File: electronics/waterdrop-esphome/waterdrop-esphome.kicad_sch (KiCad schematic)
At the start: 27 parts, among them J1 12V_IN, J2 12V_OUT, J3 Comm_RO, J4 Comm_Faucet, J5 Valve, K1 G5LE-1, Q1 BC817, U2 ESP32-S3-Tiny, U3 74AHCT125, U4 TB67H450A

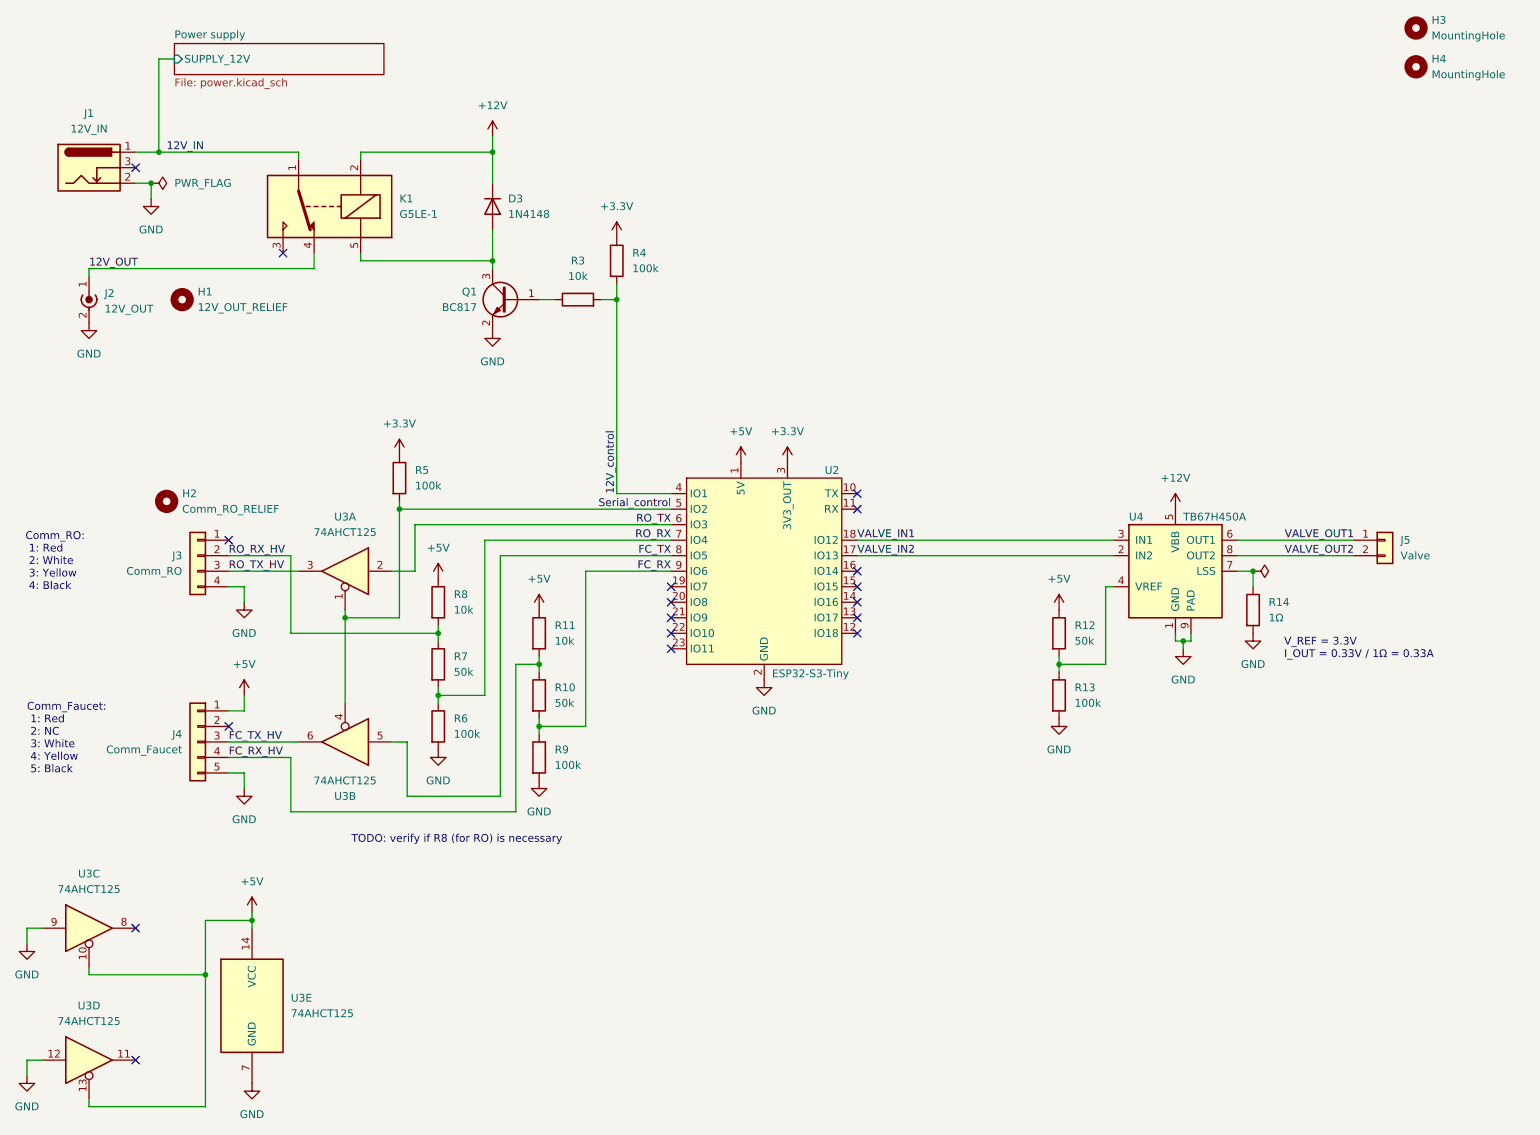
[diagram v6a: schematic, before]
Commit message: Schematics: apply verified 0.1 fixes: - Bump version to 0.2 - Change mounting holes to M3 - 12 -> 24V input voltage:   - C1: 16V -> 50V   - D1: SMAJ13A -> SMAJ30A   - D2: B220A -> B360A   - K1: G5LE-1 -> G5LE-1-E DC24 - R4: 100k -> 47k (it was too weak to fully open relay transistor) - R7/R10/R12: 50k -> 51k (more common)
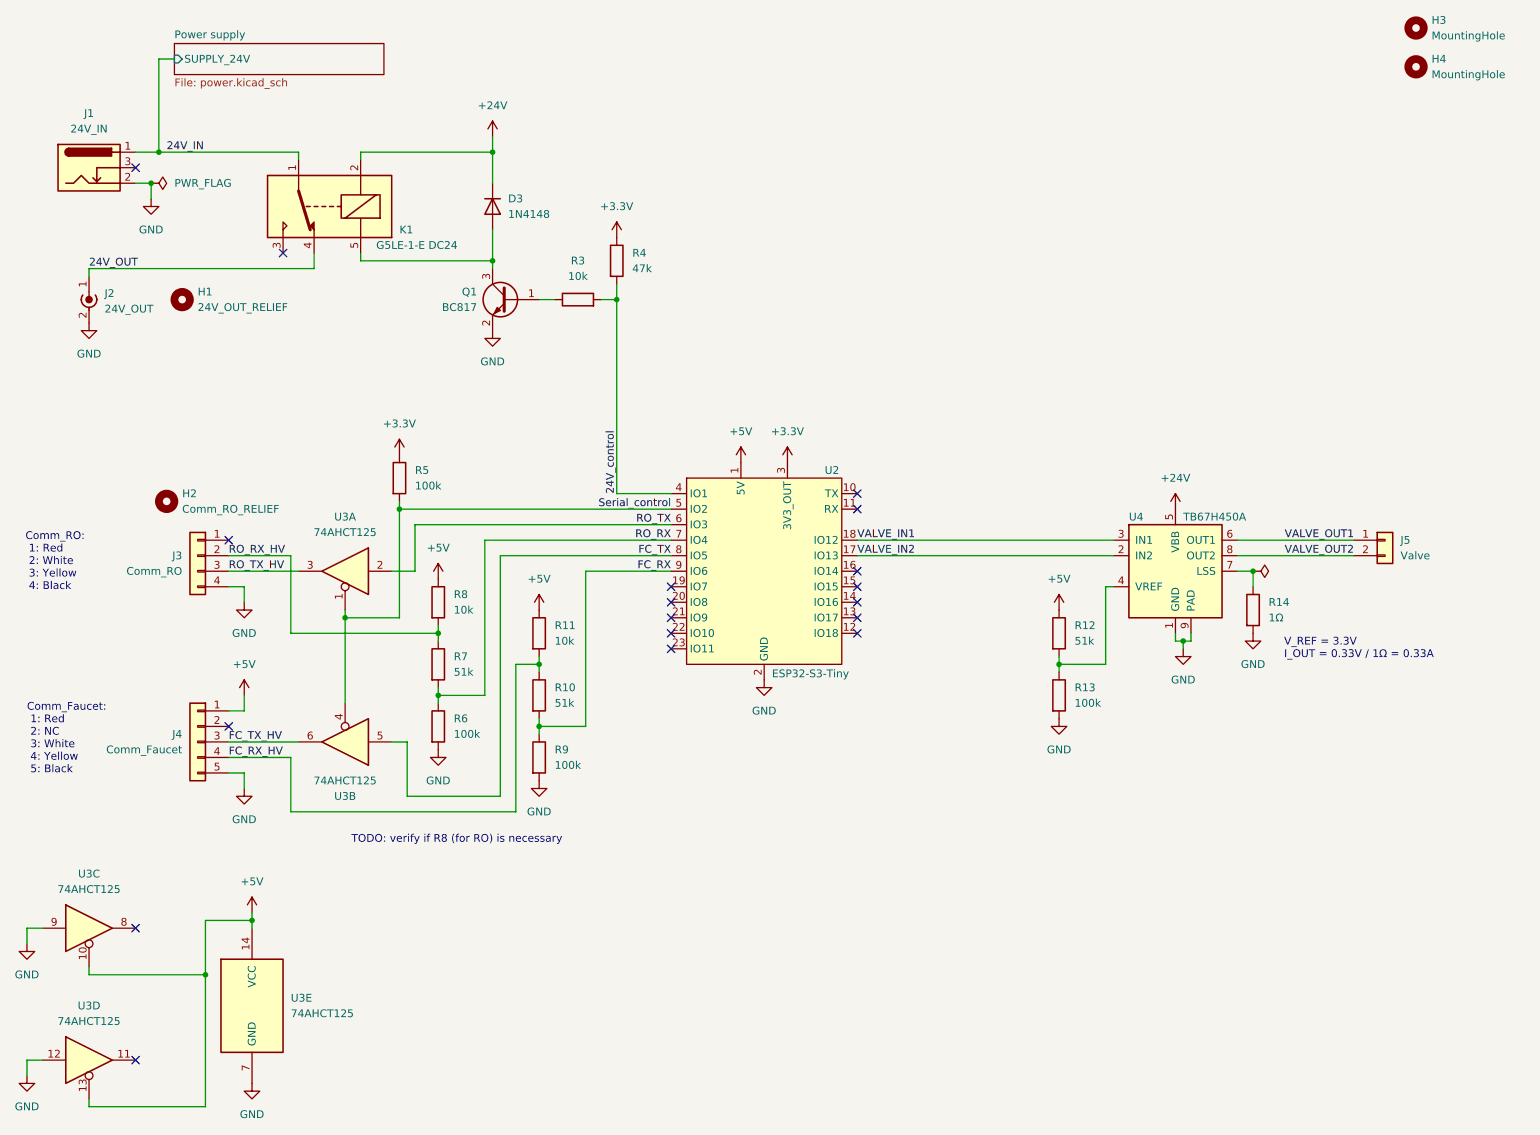
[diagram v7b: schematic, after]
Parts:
- H1: value 12V_OUT_RELIEF -> 24V_OUT_RELIEF
- H3, H4: footprint MountingHole:MountingHole_4.3mm_M4 -> MountingHole:MountingHole_3.2mm_M3
- J1: value 12V_IN -> 24V_IN
- J2: value 12V_OUT -> 24V_OUT
- K1: value G5LE-1 -> G5LE-1-E DC24
- R10, R12, R7: value 50k -> 51k
- R4: value 100k -> 47k
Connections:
- net +12V renamed +24V
- net 12V_IN renamed 24V_IN
- net 12V_OUT renamed 24V_OUT
- net 12V_control renamed 24V_control
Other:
- sheet Power supply ports: added SUPPLY_24V; removed SUPPLY_12V

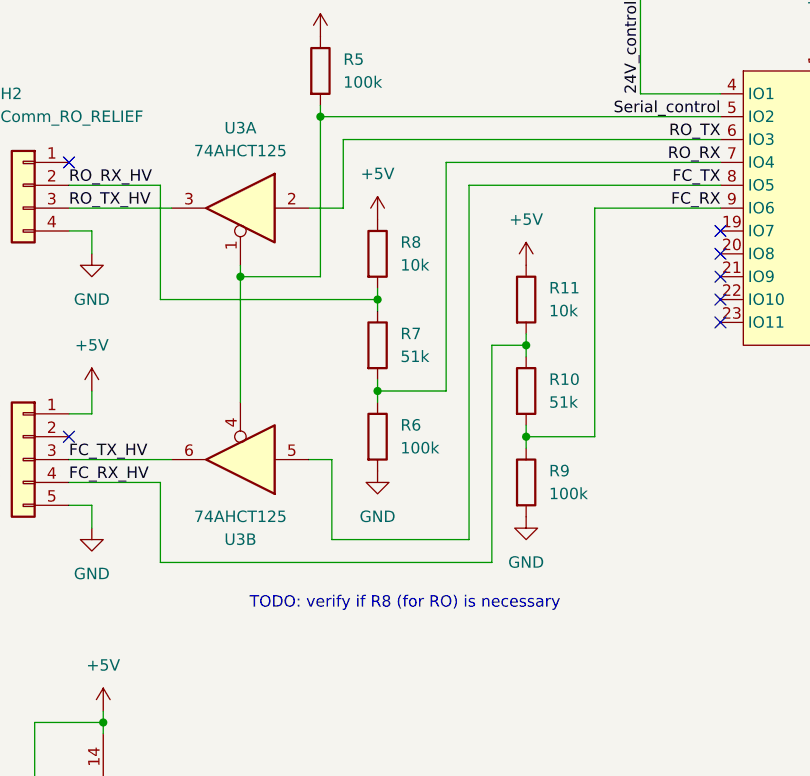
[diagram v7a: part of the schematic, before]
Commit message: Remove R8: Serial RX pull-up from RO unit
It's only necessary for faucet. Without this pull-up, this module already
performs better than original faucet. Rising and falling edge comparison
(+/- 10ns, except faucet rising edge):
- 560ns with waterdrop-esphome (both RX and TX, both edges)
- 620ns with original faucet (RO side, both edges)
- 640ns with original faucet (faucet side, falling edge)
- 10us with original faucet (faucet side, rising edge)

Faucet side rises to 3.5V after 650ns and then slowly rises to 5V in about 10us.
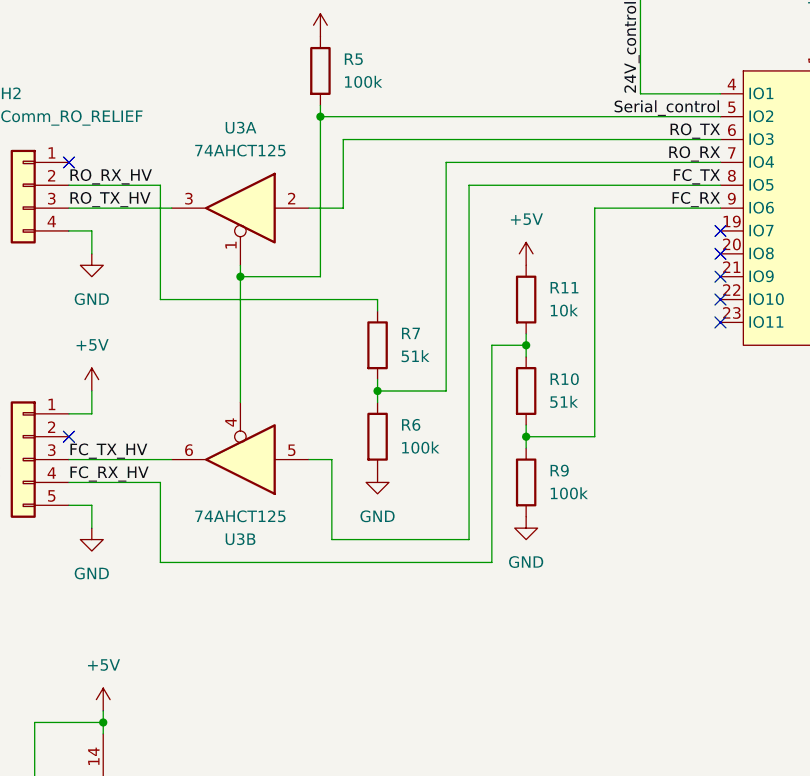
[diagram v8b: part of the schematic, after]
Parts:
- removed R8: 10k, Resistor_SMD:R_0805_2012Metric_Pad1.20x1.40mm_HandSolder, symbol Device:R
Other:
- note removed: "TODO: verify if R8 (for RO) is necessary"
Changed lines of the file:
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@@
 		)
 	)
-	(text "TODO: verify if R8 (for RO) is necessary"
-		(exclude_from_sim no)
-		(at 89.408 151.892 0)
-		(effects
-			(font
-				(size 1.27 1.27)
-			)
-		)
-	)
 	(junction
 		(at 95.25 57.15)
@@
 	)
 	(junction
-		(at 86.36 118.11)
-		(diameter 0)
-		(color 0 0 0 0)
-	)
-	(junction
 		(at 208.28 119.38)
 		(diameter 0)
@@
 	(wire
 		(pts
-			(xy 86.36 116.84) (xy 86.36 118.11)
-		)
-		(stroke
-			(width 0)
-			(type default)
-		)
-	)
-	(wire
-		(pts
 			(xy 55.88 163.83) (xy 55.88 165.1)
 		)
@@
 	(symbol
 		(lib_id "power:+5V")
-		(at 86.36 109.22 0)
-		(unit 1)
-		(exclude_from_sim no)
-		(in_bom yes)
-		(on_board yes)
-		(dnp no)
-		(fields_autoplaced yes)
-		(property "Reference" "#PWR022"
-			(at 86.36 113.03 0)
-			(effects
-				(font
-					(size 1.27 1.27)
-				)
-				(hide yes)
-			)
-		)
-		(property "Value" "+5V"
-			(at 86.36 104.14 0)
-			(effects
-				(font
-					(size 1.27 1.27)
-				)
-			)
-		)
-		(property "Footprint" ""
-			(at 86.36 109.22 0)
-			(effects
-				(font
-					(size 1.27 1.27)
-				)
-				(hide yes)
-			)
-		)
-		(property "Datasheet" ""
-			(at 86.36 109.22 0)
-			(effects
-				(font
-					(size 1.27 1.27)
-				)
-				(hide yes)
-			)
-		)
-		(property "Description" "Power symbol creates a global label with name \"+5V\""
-			(at 86.36 109.22 0)
-			(effects
-				(font
-					(size 1.27 1.27)
-				)
-				(hide yes)
-			)
-		)
-		(pin "1"
-		)
-		(instances
-			(project ""
-				(path "/35f74f22-9f08-4dab-aa3a-794dd2e7ee12"
-					(reference "#PWR022")
-					(unit 1)
-				)
-			)
-		)
-	)
-	(symbol
-		(lib_id "power:+5V")
 		(at 54.61 128.27 0)
 		(unit 1)
@@
 					(unit 1)
 				)
-			)
-		)
-	)
-	(symbol
-		(lib_id "Device:R")
-		(at 86.36 113.03 0)
-		(unit 1)
-		(exclude_from_sim no)
-		(in_bom yes)
-		(on_board yes)
-		(dnp no)
-		(fields_autoplaced yes)
-		(property "Reference" "R8"
-			(at 88.9 111.7599 0)
-			(effects
-				(font
-					(size 1.27 1.27)
-				)
-				(justify left)
-			)
-		)
-		(property "Value" "10k"
-			(at 88.9 114.2999 0)
-			(effects
-				(font
-					(size 1.27 1.27)
-				)
-				(justify left)
-			)
-		)
-		(property "Footprint" "Resistor_SMD:R_0805_2012Metric_Pad1.20x1.40mm_HandSolder"
-			(at 84.582 113.03 90)
-			(effects
-				(font
-					(size 1.27 1.27)
-				)
-				(hide yes)
-			)
-		)
-		(property "Datasheet" "~"
-			(at 86.36 113.03 0)
-			(effects
-				(font
-					(size 1.27 1.27)
-				)
-				(hide yes)
-			)
-		)
-		(property "Description" "Resistor"
-			(at 86.36 113.03 0)
-			(effects
-				(font
-					(size 1.27 1.27)
-				)
-				(hide yes)
-			)
-		)
-		(pin "1"
-		)
-		(pin "2"
-		)
-		(instances
-			(project ""
-				(path "/35f74f22-9f08-4dab-aa3a-794dd2e7ee12"
-					(reference "R8")
-					(unit 1)
-				)
